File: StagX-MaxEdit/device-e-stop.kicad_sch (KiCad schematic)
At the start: 2 parts

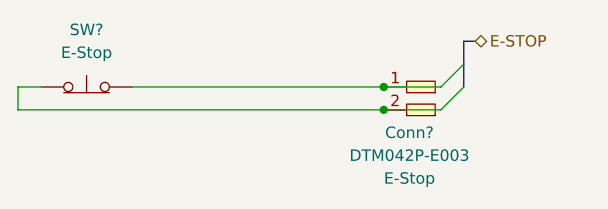
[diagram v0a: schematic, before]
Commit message: Added initial version for loom routing
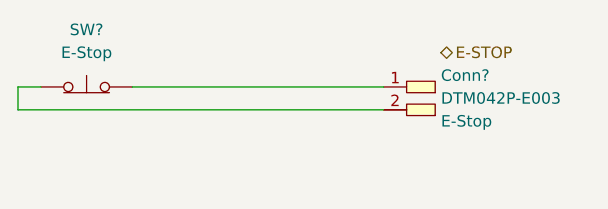
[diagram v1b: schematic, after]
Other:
- title: (none) -> DEVICE - E-STOP
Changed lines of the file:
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@@
 (kicad_sch (version 20230121) (generator eeschema)
   (paper "A4")
-  (junction (at 157.48 99.06) (diameter 0) (color 0 0 0 0)
-  )
-  (junction (at 157.48 101.6) (diameter 0) (color 0 0 0 0)
-  )
-  (bus_entry (at 163.83 101.6) (size 2.54 -2.54)
-    (stroke (width 0) (type default))
-  )
-  (bus_entry (at 163.83 99.06) (size 2.54 -2.54)
-    (stroke (width 0) (type default))
-  )
-  (bus (pts (xy 166.37 99.06) (xy 166.37 96.52))
-    (stroke (width 0) (type default))
-  )
-  (wire (pts (xy 157.48 99.06) (xy 163.83 99.06))
-    (stroke (width 0) (type default))
+  (title_block
+    (title "DEVICE - E-STOP")
   )
   (wire (pts (xy 119.38 99.06) (xy 116.84 99.06))
@@
     (stroke (width 0) (type default))
   )
-  (bus (pts (xy 166.37 96.52) (xy 166.37 93.98))
-    (stroke (width 0) (type default))
-  )
-  (wire (pts (xy 157.48 101.6) (xy 163.83 101.6))
-    (stroke (width 0) (type default))
-  )
   (wire (pts (xy 129.54 99.06) (xy 157.48 99.06))
     (stroke (width 0) (type default))
   )
-  (bus (pts (xy 166.37 93.98) (xy 167.64 93.98))
-    (stroke (width 0) (type default))
-  )
-  (hierarchical_label "E-STOP" (shape bidirectional) (at 167.64 93.98 0) (fields_autoplaced)
+  (hierarchical_label "E-STOP" (shape bidirectional) (at 163.83 95.25 0) (fields_autoplaced)
     (effects (font (size 1.27 1.27)) (justify left))
   )
@@
   (symbol (lib_id "Connectors_SUFST:Deutsch_DTM_2P_Pin") (at 159.385 106.045 180) (unit 1)
     (in_bom yes) (on_board yes) (dnp no) (fields_autoplaced)
-    (property "Reference" "Conn?" (at 160.3375 104.14 0)
-      (effects (font (size 1.27 1.27)))
+    (property "Reference" "Conn?" (at 163.83 97.79 0)
+      (effects (font (size 1.27 1.27)) (justify right))
     )
     (property "Value" "Deutsch_DTM_2P_Pin" (at 159.385 106.045 0)
@@
       (effects (font (size 1.27 1.27)) hide)
     )
-    (property "P/N" "DTM042P-E003" (at 160.3375 106.68 0)
-      (effects (font (size 1.27 1.27)))
+    (property "P/N" "DTM042P-E003" (at 163.83 100.33 0)
+      (effects (font (size 1.27 1.27)) (justify right))
     )
-    (property "Conn Name" "E-Stop" (at 160.3375 109.22 0)
-      (effects (font (size 1.27 1.27)))
+    (property "Conn Name" "E-Stop" (at 163.83 102.87 0)
+      (effects (font (size 1.27 1.27)) (justify right))
     )
     (pin "1")
